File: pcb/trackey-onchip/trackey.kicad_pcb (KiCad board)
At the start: 2 copper layers, 49.5 x 77.5 mm, 34 parts, among them J1 USB, J10 ROW_port, J11 COL_port, J2 Jack, J9 Trackball_port, SW1 RST_SW, SW2 i2c/RS232, SW3 i2c/RS232, SW4 slave/master, SW5 slave/master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

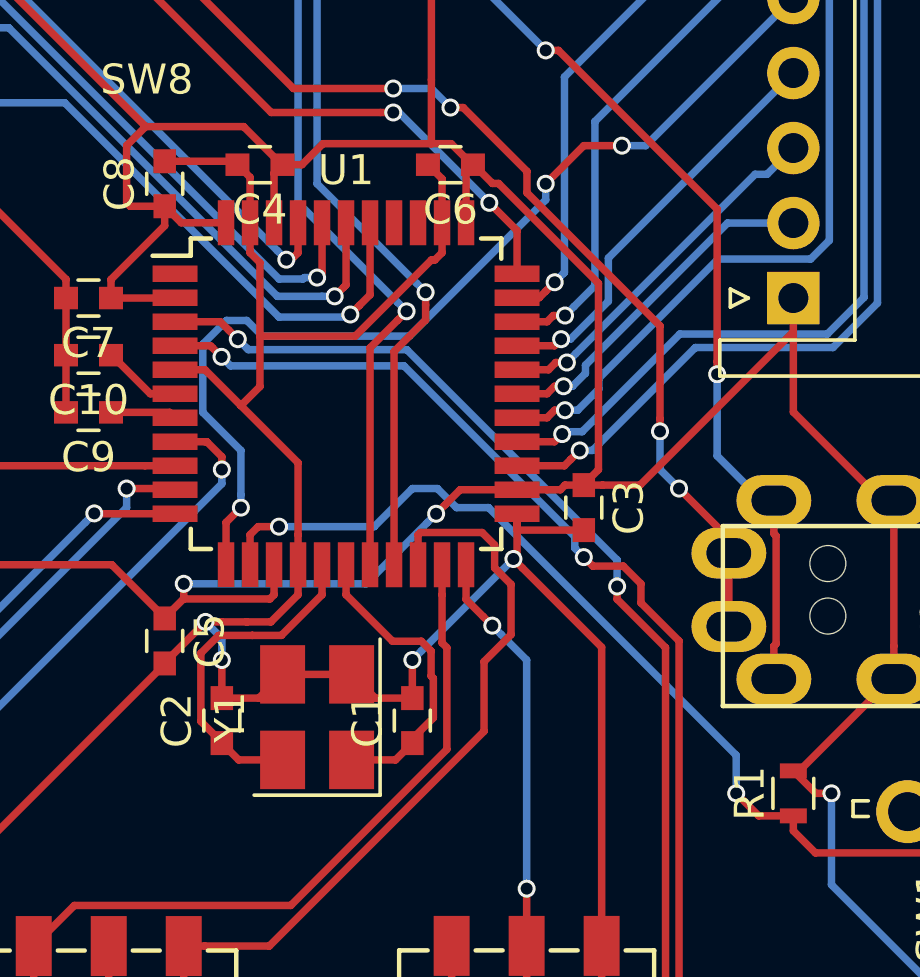
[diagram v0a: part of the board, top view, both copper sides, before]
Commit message: wiring trackey-onchip
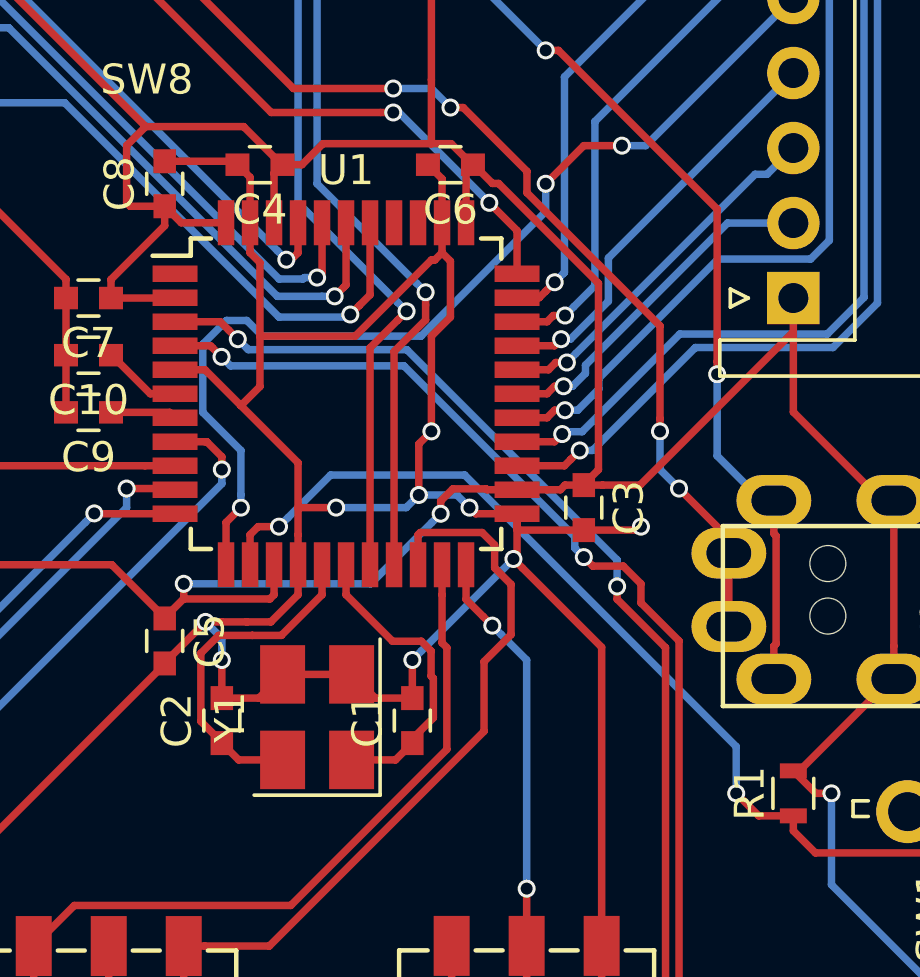
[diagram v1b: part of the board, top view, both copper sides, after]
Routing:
- net GND: track 241.4 -> 259.7 mm, vias 6 -> 11
- net /RST: track 32.2 -> 32.7 mm
